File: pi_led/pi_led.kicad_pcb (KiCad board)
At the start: 2 copper layers, 50 x 50 mm, 13 parts, among them CON1 PWR, P1 LED_STRIP, P2 RiPi, Q1 STP16NF06L, Q2 STP16NF06L, Q3 STP16NF06L

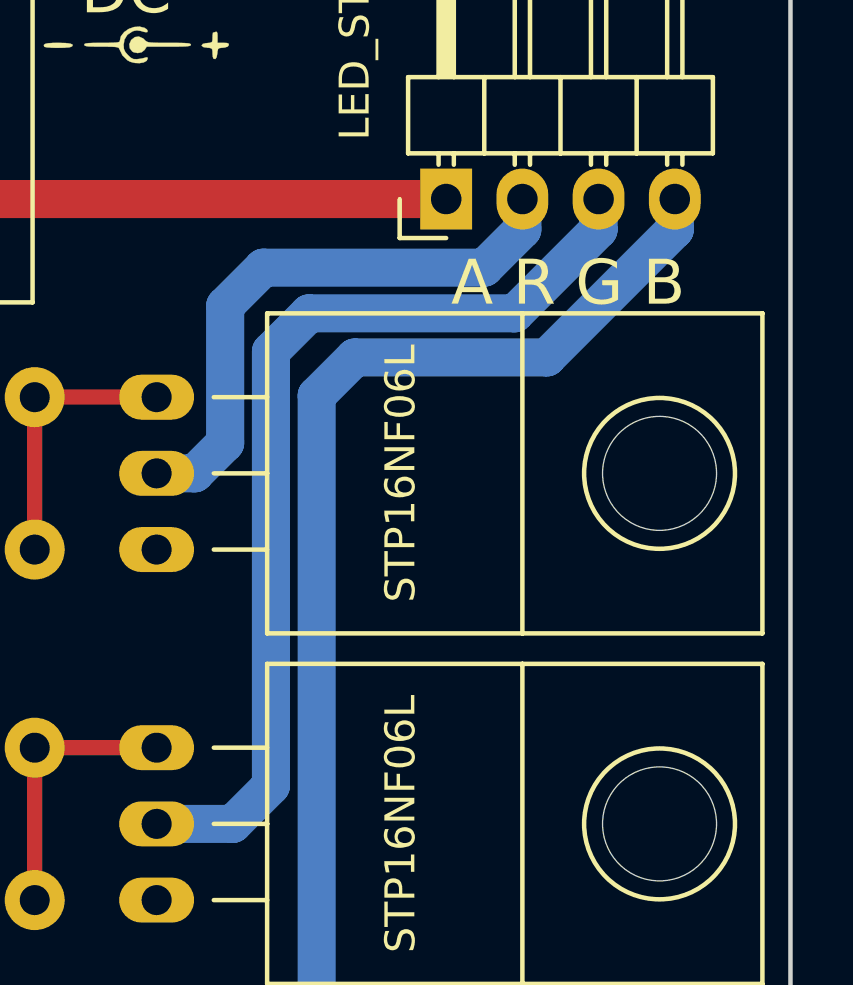
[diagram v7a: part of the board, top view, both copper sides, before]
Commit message: Track corner best practices
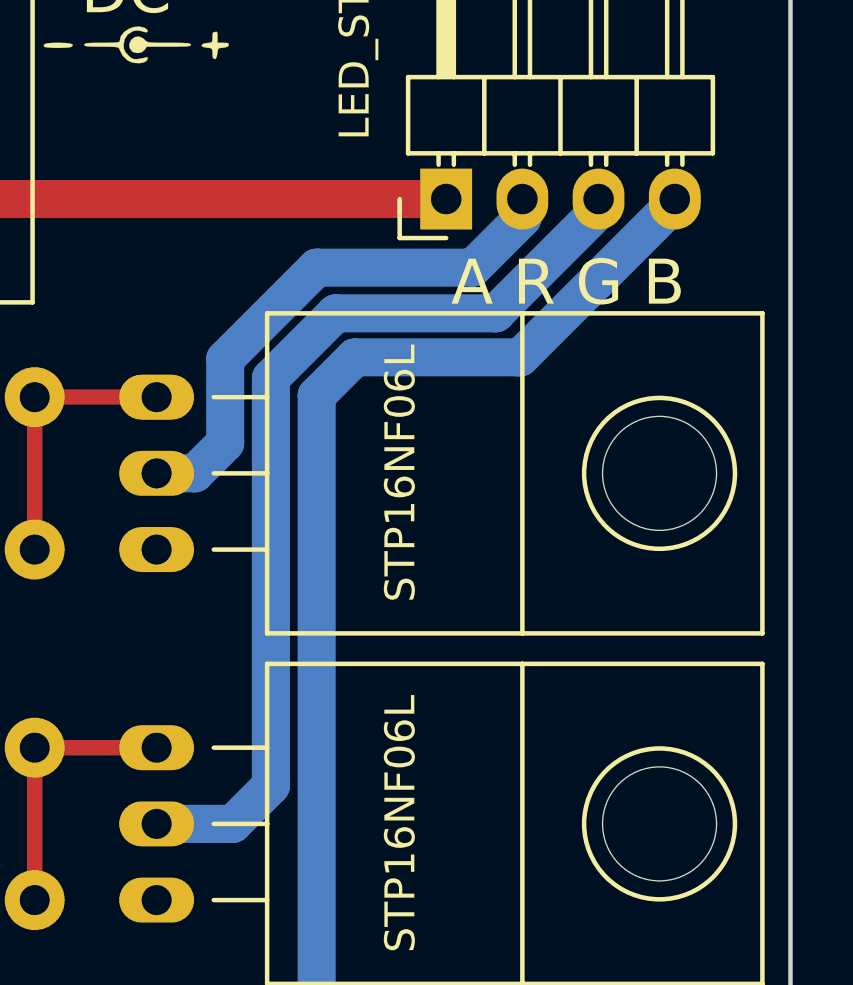
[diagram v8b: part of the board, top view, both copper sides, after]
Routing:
- net /LED_R: track 19.3 -> 18.0 mm
- net /LED_G: track 32.4 -> 31.5 mm
- net /LED_B: track 45.8 -> 45.3 mm
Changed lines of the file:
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@@
   (segment (start 110.236 73.76414) (end 112.88014 71.12) (width 1.27) (layer F.Cu) (net 1))
   (segment (start 112.88014 71.12) (end 128.524 71.12) (width 1.27) (layer F.Cu) (net 1))
-  (segment (start 131.064 71.12) (end 131.064 72.136) (width 1.27) (layer B.Cu) (net 3))
-  (segment (start 131.064 72.136) (end 129.794 73.406) (width 1.27) (layer B.Cu) (net 3))
-  (segment (start 129.794 73.406) (end 122.428 73.406) (width 1.27) (layer B.Cu) (net 3))
-  (segment (start 122.428 73.406) (end 121.158 74.676) (width 1.27) (layer B.Cu) (net 3))
-  (segment (start 121.158 74.676) (end 121.158 79.248) (width 1.27) (layer B.Cu) (net 3))
+  (segment (start 131.064 71.12) (end 131.064 71.755) (width 1.27) (layer B.Cu) (net 3) (status 400000))
+  (segment (start 131.064 71.755) (end 129.413 73.406) (width 1.27) (layer B.Cu) (net 3))
+  (segment (start 129.413 73.406) (end 124.206 73.406) (width 1.27) (layer B.Cu) (net 3))
+  (segment (start 124.206 73.406) (end 121.158 76.454) (width 1.27) (layer B.Cu) (net 3))
+  (segment (start 121.158 76.454) (end 121.158 79.248) (width 1.27) (layer B.Cu) (net 3))
   (segment (start 121.158 79.248) (end 120.142 80.264) (width 1.27) (layer B.Cu) (net 3))
   (segment (start 120.142 80.264) (end 118.872 80.264) (width 1.27) (layer B.Cu) (net 3))
-  (segment (start 133.604 71.12) (end 133.604 72.136) (width 1.27) (layer B.Cu) (net 4))
+  (segment (start 133.604 71.12) (end 133.604 71.501) (width 1.27) (layer B.Cu) (net 4) (status 400000))
   (segment (start 121.412 91.948) (end 118.872 91.948) (width 1.27) (layer B.Cu) (net 4))
   (segment (start 122.682 90.678) (end 121.412 91.948) (width 1.27) (layer B.Cu) (net 4))
-  (segment (start 122.682 76.2) (end 122.682 90.678) (width 1.27) (layer B.Cu) (net 4))
-  (segment (start 123.952 74.93) (end 122.682 76.2) (width 1.27) (layer B.Cu) (net 4))
-  (segment (start 130.81 74.93) (end 123.952 74.93) (width 1.27) (layer B.Cu) (net 4))
-  (segment (start 133.604 72.136) (end 130.81 74.93) (width 1.27) (layer B.Cu) (net 4))
-  (segment (start 136.144 71.12) (end 136.144 72.136) (width 1.27) (layer B.Cu) (net 5))
+  (segment (start 122.682 77.089) (end 122.682 90.678) (width 1.27) (layer B.Cu) (net 4))
+  (segment (start 124.841 74.93) (end 122.682 77.089) (width 1.27) (layer B.Cu) (net 4))
+  (segment (start 130.175 74.93) (end 124.841 74.93) (width 1.27) (layer B.Cu) (net 4))
+  (segment (start 133.604 71.501) (end 130.175 74.93) (width 1.27) (layer B.Cu) (net 4))
+  (segment (start 136.144 71.12) (end 136.144 71.247) (width 1.27) (layer B.Cu) (net 5) (status 400000))
   (segment (start 122.936 103.632) (end 118.872 103.632) (width 1.27) (layer B.Cu) (net 5))
   (segment (start 124.206 102.362) (end 122.936 103.632) (width 1.27) (layer B.Cu) (net 5))
   (segment (start 124.206 77.670002) (end 124.206 102.362) (width 1.27) (layer B.Cu) (net 5))
   (segment (start 125.476 76.400002) (end 124.206 77.670002) (width 1.27) (layer B.Cu) (net 5))
-  (segment (start 131.879998 76.400002) (end 125.476 76.400002) (width 1.27) (layer B.Cu) (net 5))
-  (segment (start 136.144 72.136) (end 131.879998 76.400002) (width 1.27) (layer B.Cu) (net 5))
+  (segment (start 130.990998 76.400002) (end 125.476 76.400002) (width 1.27) (layer B.Cu) (net 5))
+  (segment (start 136.144 71.247) (end 130.990998 76.400002) (width 1.27) (layer B.Cu) (net 5))
   (segment (start 94.996 104.14) (end 98.044 101.092) (width 0.508) (layer F.Cu) (net 6))
   (segment (start 98.044 101.092) (end 104.648 101.092) (width 0.508) (layer F.Cu) (net 6))
@@
     (polygon
       (pts
-        (xy 139.5 109.5) (xy 130.5 109.5) (xy 131 77.5) (xy 131.5 77.5) (xy 132.5 77)
-        (xy 134 75.5) (xy 139.5 75.5)
+        (xy 139.5 109.5) (xy 130.5 109.5) (xy 131 77.5) (xy 133 75.5) (xy 139.5 75.5)
       )
     )
